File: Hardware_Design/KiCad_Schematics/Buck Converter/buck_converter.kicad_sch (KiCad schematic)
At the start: 3 parts, among them J1 Conn_01x02_Socket, J2 Conn_01x01_Pin, J3 Conn_01x02_Socket

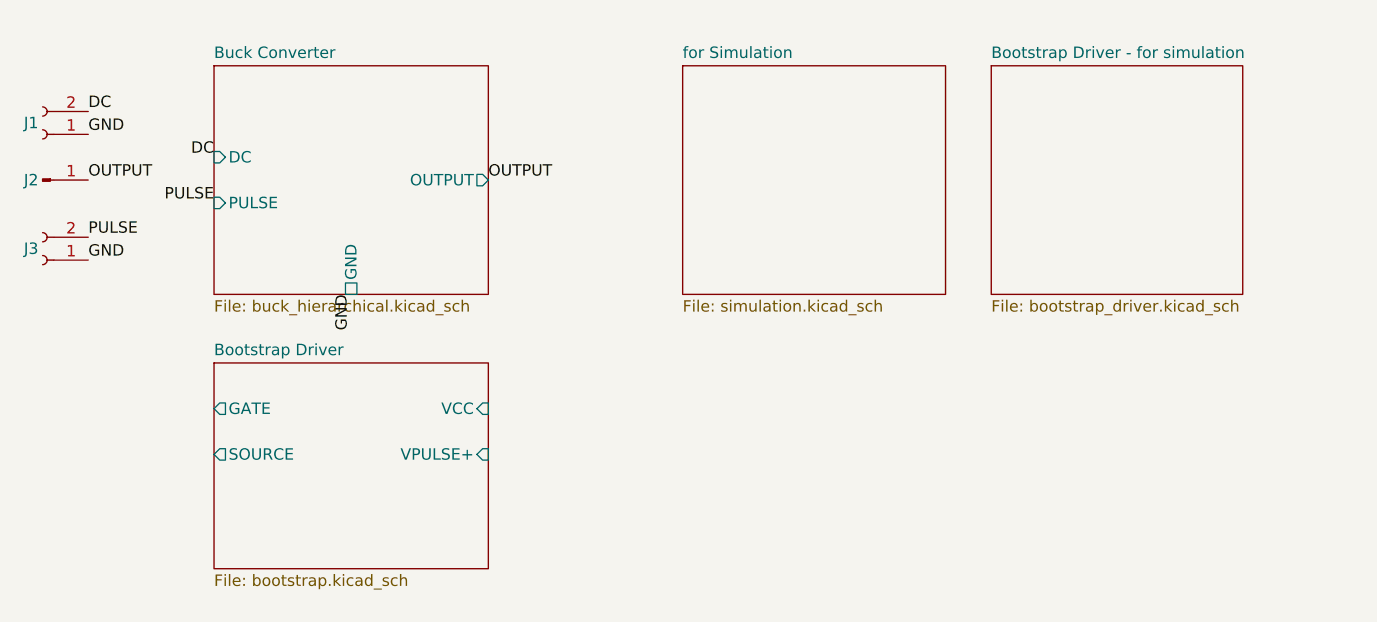
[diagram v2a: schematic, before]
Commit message: Update designs but continue problems...
Added a Bootstrap circuit to bring the MOSFET from a Linear Regulator state to a Buck Converter state, but the problem is still not resolved. While it should yield a value close to 6V when the Duty Cycle is at 50% and a 12V input is applied, it yields 4V, and the graph is not correct. Work on the problem will continue.
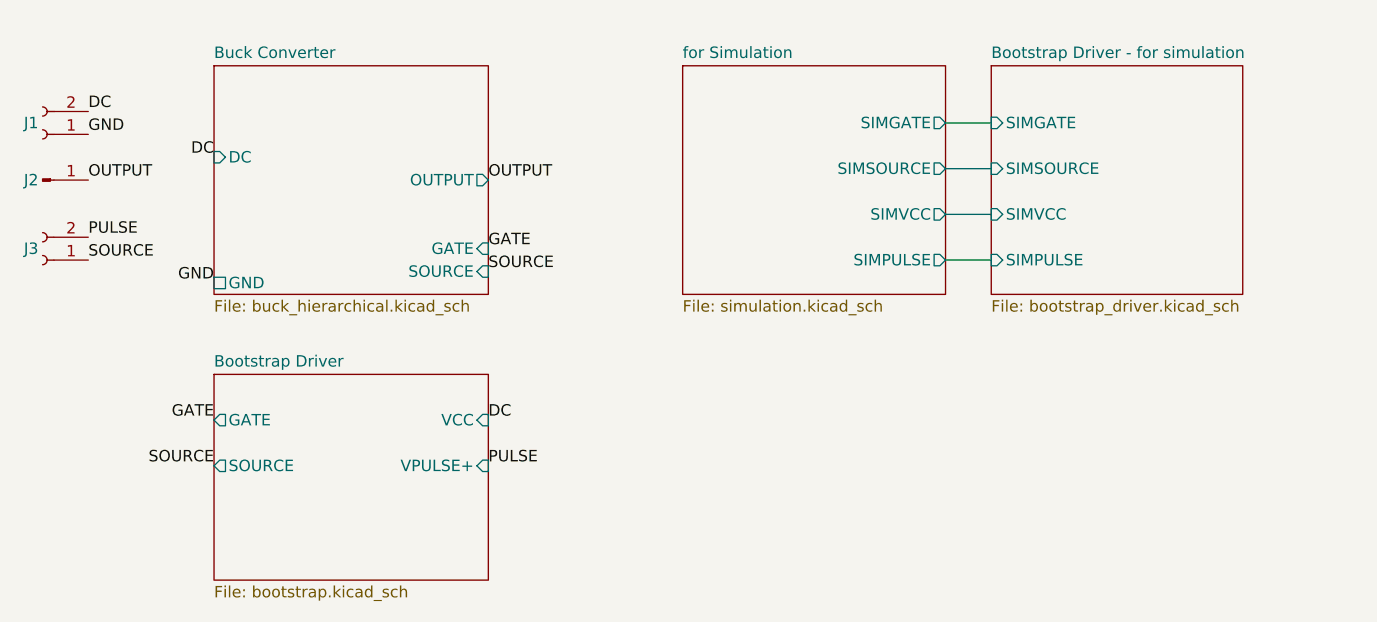
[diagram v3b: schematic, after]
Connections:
- net GND: no longer J3.1 (Pin_1)
- new net SOURCE: J3.1 (Pin_1)
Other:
- sheet Bootstrap Driver - for simulation ports: added SIMGATE, SIMPULSE, SIMSOURCE, SIMVCC; removed none
- sheet Buck Converter ports: added GATE, SOURCE; removed PULSE
- sheet for Simulation ports: added SIMGATE, SIMPULSE, SIMSOURCE, SIMVCC; removed none
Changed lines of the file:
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@@
 	(generator_version "10.0")
 	(paper "A4")
+	(wire
+		(pts
+			(xy 176.53 107.95) (xy 181.61 107.95)
+		)
+		(stroke
+			(width 0)
+			(type default)
+		)
+	)
+	(wire
+		(pts
+			(xy 176.53 113.03) (xy 181.61 113.03)
+		)
+		(stroke
+			(width 0)
+			(type default)
+		)
+	)
+	(wire
+		(pts
+			(xy 176.53 97.79) (xy 181.61 97.79)
+		)
+		(stroke
+			(width 0)
+			(type default)
+		)
+	)
+	(wire
+		(pts
+			(xy 176.53 102.87) (xy 181.61 102.87)
+		)
+		(stroke
+			(width 0)
+			(type default)
+		)
+	)
+	(label "DC"
+		(at 125.73 130.81 0)
+		(effects
+			(font
+				(size 1.27 1.27)
+			)
+			(justify left bottom)
+		)
+	)
 	(label "GND"
 		(at 81.28 99.06 0)
@@
 		)
 	)
-	(label "GND"
-		(at 110.49 116.84 270)
+	(label "SOURCE"
+		(at 81.28 113.03 0)
+		(effects
+			(font
+				(size 1.27 1.27)
+			)
+			(justify left bottom)
+		)
+	)
+	(label "SOURCE"
+		(at 95.25 135.89 180)
+		(effects
+			(font
+				(size 1.27 1.27)
+			)
+			(justify right bottom)
+		)
+	)
+	(label "SOURCE"
+		(at 125.73 114.3 0)
+		(effects
+			(font
+				(size 1.27 1.27)
+			)
+			(justify left bottom)
+		)
+	)
+	(label "GATE"
+		(at 95.25 130.81 180)
 		(effects
 			(font
@@
 		)
 	)
-	(label "GND"
-		(at 81.28 113.03 0)
-		(effects
-			(font
-				(size 1.27 1.27)
-			)
-			(justify left bottom)
-		)
-	)
 	(label "OUTPUT"
 		(at 125.73 104.14 0)
@@
 		)
 	)
+	(label "PULSE"
+		(at 125.73 135.89 0)
+		(effects
+			(font
+				(size 1.27 1.27)
+			)
+			(justify left bottom)
+		)
+	)
 	(label "DC"
 		(at 95.25 101.6 180)
@@
 		)
 	)
-	(label "PULSE"
-		(at 95.25 106.68 180)
+	(label "GND"
+		(at 95.25 115.57 180)
 		(effects
 			(font
@@
 			)
 			(justify right bottom)
+		)
+	)
+	(label "GATE"
+		(at 125.73 111.76 0)
+		(effects
+			(font
+				(size 1.27 1.27)
+			)
+			(justify left bottom)
 		)
 	)
@@
 			)
 		)
+		(pin "SIMGATE" input
+			(at 181.61 97.79 180)
+			(effects
+				(font
+					(size 1.27 1.27)
+				)
+				(justify left)
+			)
+		)
+		(pin "SIMPULSE" input
+			(at 181.61 113.03 180)
+			(effects
+				(font
+					(size 1.27 1.27)
+				)
+				(justify left)
+			)
+		)
+		(pin "SIMSOURCE" input
+			(at 181.61 102.87 180)
+			(effects
+				(font
+					(size 1.27 1.27)
+				)
+				(justify left)
+			)
+		)
+		(pin "SIMVCC" input
+			(at 181.61 107.95 180)
+			(effects
+				(font
+					(size 1.27 1.27)
+				)
+				(justify left)
+			)
+		)
 		(instances
 			(project "buck_converter"
@@
 			)
 		)
+		(pin "SIMGATE" output
+			(at 176.53 97.79 0)
+			(effects
+				(font
+					(size 1.27 1.27)
+				)
+				(justify right)
+			)
+		)
+		(pin "SIMSOURCE" output
+			(at 176.53 102.87 0)
+			(effects
+				(font
+					(size 1.27 1.27)
+				)
+				(justify right)
+			)
+		)
+		(pin "SIMVCC" output
+			(at 176.53 107.95 0)
+			(effects
+				(font
+					(size 1.27 1.27)
+				)
+				(justify right)
+			)
+		)
+		(pin "SIMPULSE" output
+			(at 176.53 113.03 0)
+			(effects
+				(font
+					(size 1.27 1.27)
+				)
+				(justify right)
+			)
+		)
 		(instances
 			(project "buck_converter"
@@
 	)
 	(sheet
-		(at 95.25 124.46)
+		(at 95.25 125.73)
 		(size 30.48 22.86)
 		(exclude_from_sim yes)
@@
 		)
 		(property "Sheetname" "Bootstrap Driver"
-			(at 95.25 123.7484 0)
+			(at 95.25 125.0184 0)
 			(show_name no)
 			(do_not_autoplace no)
@@
 		)
 		(property "Sheetfile" "bootstrap.kicad_sch"
-			(at 95.25 147.9046 0)
+			(at 95.25 149.1746 0)
 			(show_name no)
 			(do_not_autoplace no)
@@
 		)
 		(pin "GATE" output
-			(at 95.25 129.54 180)
+			(at 95.25 130.81 180)
 			(effects
 				(font
@@
 		)
 		(pin "SOURCE" output
-			(at 95.25 134.62 180)
+			(at 95.25 135.89 180)
 			(effects
 				(font
@@
 		)
 		(pin "VCC" input
-			(at 125.73 129.54 0)
+			(at 125.73 130.81 0)
 			(effects
 				(font
@@
 		)
 		(pin "VPULSE+" input
-			(at 125.73 134.62 0)
+			(at 125.73 135.89 0)
 			(effects
 				(font
@@
 			)
 		)
-		(pin "PULSE" input
-			(at 95.25 106.68 180)
-			(effects
-				(font
-					(size 1.27 1.27)
-				)
-				(justify left)
+		(pin "GATE" input
+			(at 125.73 111.76 0)
+			(effects
+				(font
+					(size 1.27 1.27)
+				)
+				(justify right)
+			)
+		)
+		(pin "SOURCE" input
+			(at 125.73 114.3 0)
+			(effects
+				(font
+					(size 1.27 1.27)
+				)
+				(justify right)
 			)
 		)
 		(pin "GND" passive
-			(at 110.49 116.84 270)
-			(effects
-				(font
+			(at 95.25 115.57 180)
+			(effects
+				(font
